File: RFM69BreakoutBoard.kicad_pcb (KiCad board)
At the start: 2 copper layers, 25.7 x 25.4 mm, 16 parts, among them P1 CONN_7, U1 MCP1703, U2 74LVC2, U3 74AHC1G, U4 RFM69HW

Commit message: clean up
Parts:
- removed D2, D3: LED-GREEN, LED-0805
- removed R3, R4: 0, SM0805
- removed R5: 270, SM0805
- removed U4: RFM69HW, RFM69HW
- added C4: 10u, 10uCap, F.Cu at (107.4, 150.2)
- added C5: .1u, SM0805, F.Cu at (99.6, 149.1)
- added P11: ANA hole, PINTST, F.Cu at (106.7, 143.0)
- added W1: TEST, SMTST, F.Cu at (82.9, 158.9)
- added W2: TEST, SMTST, F.Cu at (102.7, 158.8)
- added W3: TEST, SMTST, F.Cu at (98.0, 158.9)
- added W4: TEST, SMTST, F.Cu at (107.3, 158.9)
- added W5: TEST, SMTST, F.Cu at (93.1, 158.9)
- added W6: TEST, SMTST, F.Cu at (88.0, 158.9)
- added W7: TEST, SMTST, F.Cu at (90.2, 141.1)
- added W8: TEST, SMTST, F.Cu at (94.6, 141.0)
- added W9: TEST, SMTST, F.Cu at (99.4, 141.0)
- C1, C3, U1: moved to F.Cu
- C2: footprint SM0805 -> 10uCap; moved to F.Cu
- D1: value LED-GREEN -> LED
- P1: value CONN_7 -> BB Holes
- R1: value 270 -> 10K; moved to F.Cu
- R2: value 270 -> 470; moved to F.Cu
- U2: value 74LVC2 -> 74LVC245; moved to F.Cu
- U3: value 74AHC1G -> RFM69HW; footprint SOT353 -> RFM69HW
- moved R1 19.2 mm to (89.5, 155.4), turned to 90 degrees
- moved U3 14.7 mm to (94.7, 147.3), turned to 0 degrees
- moved R2 11.2 mm to (99.3, 143.9), turned to 0 degrees
- moved C2 9.88 mm to (82.8, 150.0)
- moved C3 9.44 mm to (95.5, 151.6)
- moved D1 9.25 mm to (99.1, 146.1)
- moved U1 9.02 mm to (93.1, 152.1), turned to 180 degrees
- moved U2 8.81 mm to (92.8, 146.6), turned to 0 degrees
- moved C1 6.59 mm to (95.5, 153.8)
- moved P1 0.28 mm to (95.8, 162.8)
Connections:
- D1 pad 1: /MISO -> N-0000010
- D1 pad 2: /LED -> N-0000011
- P1 pad 1: /5V -> +5V
- P1 pad 3: /CLK -> /CLK_5V
- P1 pad 5: /MOSI -> /MOSI_5V
- P1 pad 6: /CS -> /CS_5V
- R1 pad 1: /LED -> /CS_5V
- R1 pad 2: GND -> +5V
- R2 pad 1: /LED -> N-0000011
- R2 pad 2: GND -> /CS_3V3
- U2 pad 1: (no net) -> +3.3V
- U2 pad 15: (no net) -> N-0000010
- U2 pad 16: /CS -> /CS_3V3
- U2 pad 17: /MOSI -> /MOSI_3V3
- U2 pad 18: /CLK -> /CLK_3V3
- U2 pad 2: /CLK -> N-000004
- U2 pad 3: /MOSI -> N-000007
- U2 pad 4: /CS -> N-000008
- U2 pad 5: (no net) -> N-000004
- U2 pad 6: (no net) -> GND
- U2 pad 7: (no net) -> GND
- U2 pad 8: (no net) -> GND
- U2 pad 9: (no net) -> GND
- U3 pad 1: /CS -> (no net)
- U3 pad 2: /MISO -> N-000001
- U3 pad 3: GND -> (no net)
- U3 pad 4: /MISO -> (no net)
- U3 pad 5: +3.3V -> (no net)
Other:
- board size 25.7 x 25.4 mm -> 30 x 25.9 mm

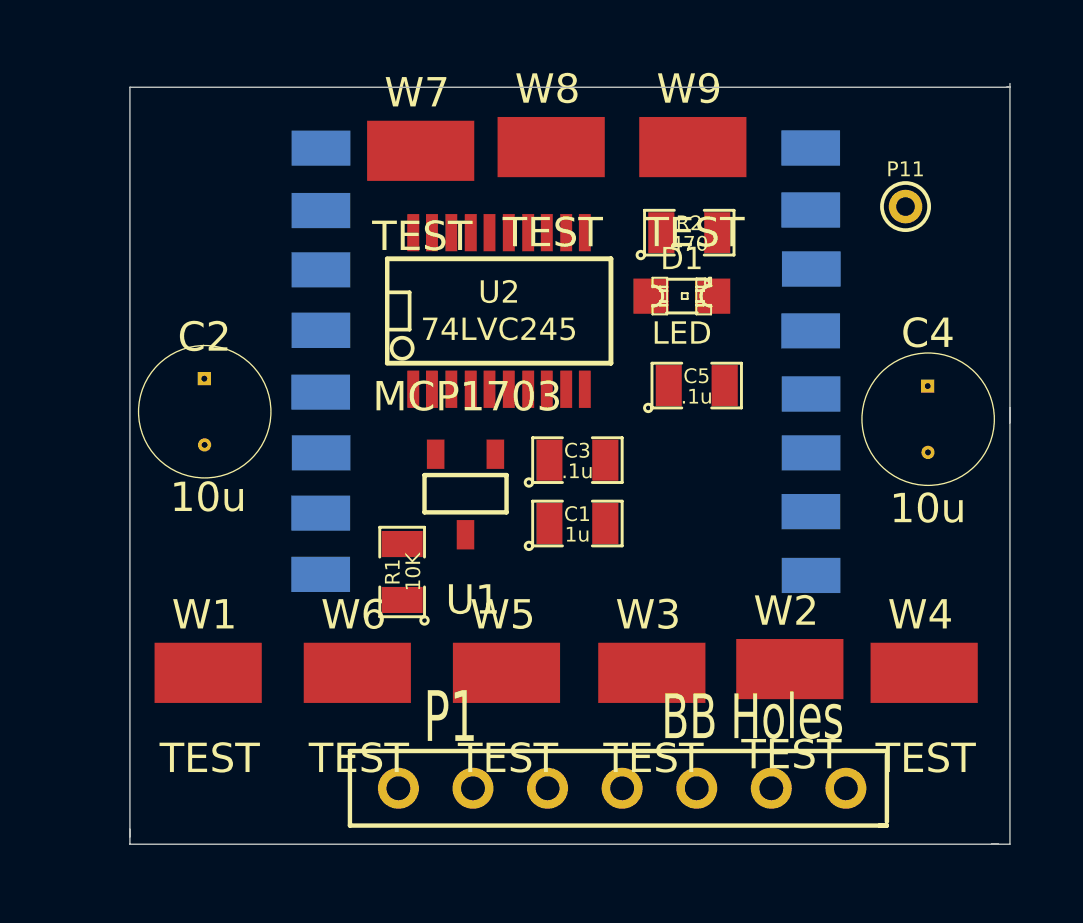
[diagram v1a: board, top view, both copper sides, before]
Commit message: started work on pcb layout
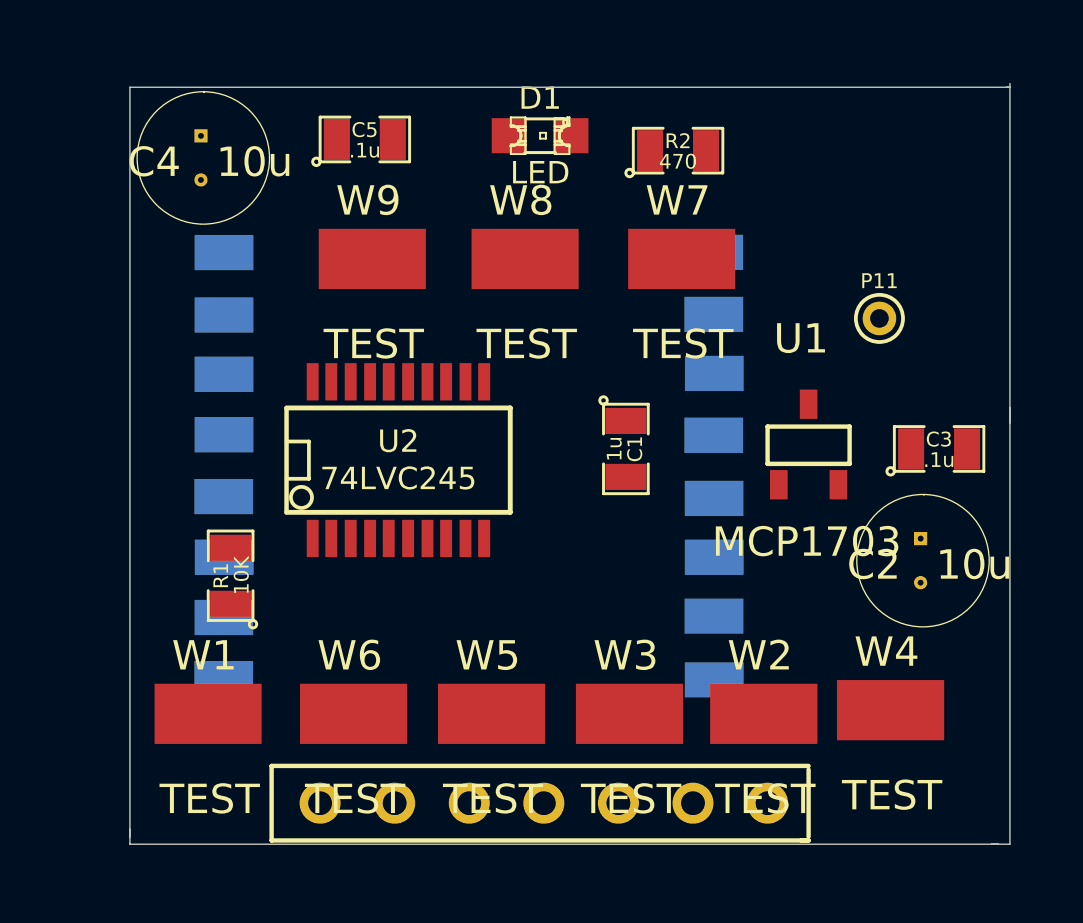
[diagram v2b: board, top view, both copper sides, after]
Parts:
- removed P1: BB Holes, 7_PINS
- added ?: , 7_PINS, F.Cu at (93.1, 163.3)
- moved C4 26.2 mm to (82.7, 141.6)
- moved C2 25.0 mm to (107.2, 155.3)
- moved C5 14.1 mm to (88.3, 140.7)
- moved C3 12.3 mm to (107.8, 151.3)
- moved W9 11.6 mm to (88.5, 144.8)
- moved W7 9.62 mm to (99.1, 144.8)
- moved U1 8.90 mm to (102.0, 151.8), turned to 0 degrees
- moved D1 7.29 mm to (94.2, 140.6)
- moved U2 6.13 mm to (89.4, 151.6)
- moved R1 5.84 mm to (83.7, 155.6)
- moved U3 4.85 mm to (91.4, 150.9)
- moved P11 3.91 mm to (105.8, 146.8)
- moved W8 3.91 mm to (93.7, 144.8)
- moved C1 3.03 mm to (97.2, 151.3), turned to 270 degrees
- moved R2 2.82 mm to (98.9, 141.1)
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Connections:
- net N-0000032 renamed /ANA
- D1 pad 1: N-0000010 -> /CLK_3V3
- D1 pad 2: N-0000011 -> /CLK_3V3
- R2 pad 1: N-0000011 -> /CLK_3V3
- U2 pad 15: N-0000010 -> /CLK_3V3
- U2 pad 2: N-000004 -> /CLK_5V
- U2 pad 3: N-000007 -> /MOSI_5V
- U2 pad 4: N-000008 -> /CS_5V
- U2 pad 5: N-000004 -> /CLK_5V
- U3 pad 11: N-000003 -> GND
- U3 pad 12: /CS_3V3 -> /CLK_3V3
- U3 pad 13: N-000006 -> /MISO
- U3 pad 14: N-000005 -> /MOSI_3V3
- U3 pad 15: N-000002 -> /CS_3V3
- U3 pad 2: N-000001 -> /INT
- U3 pad 9: N-000003 -> GND

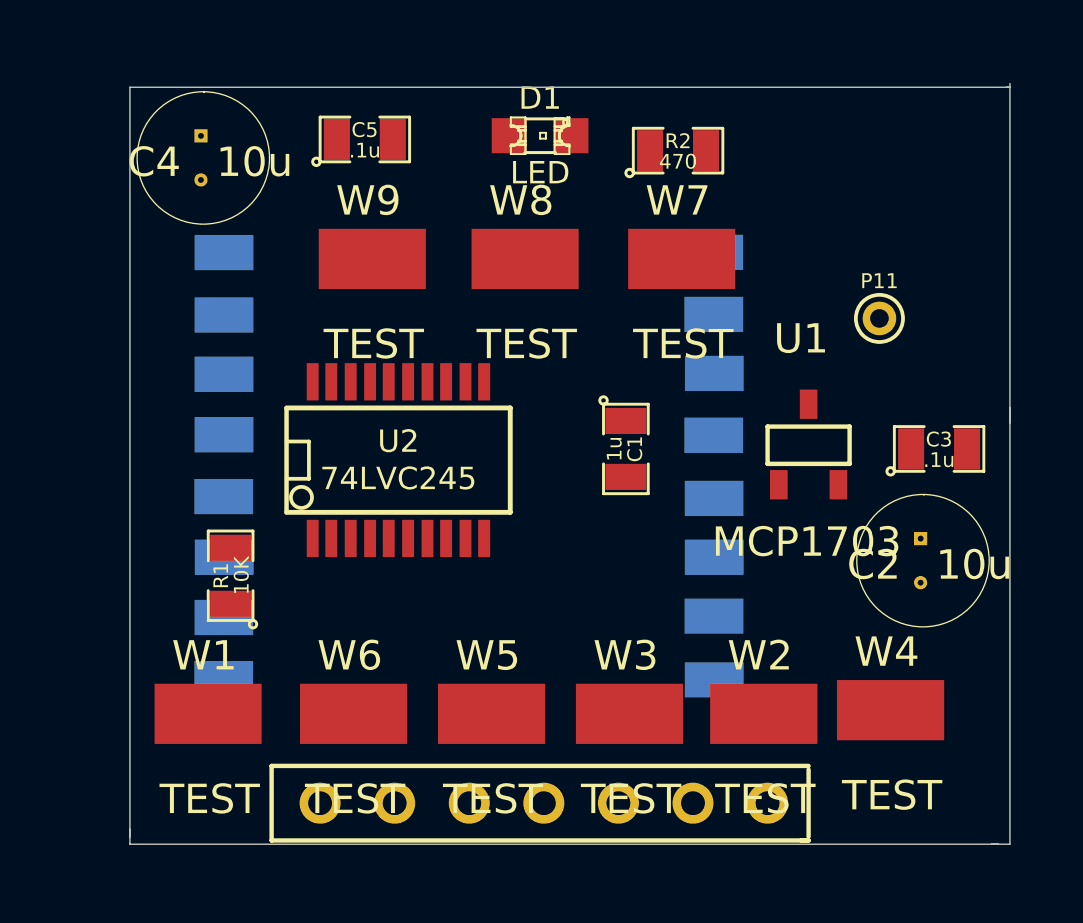
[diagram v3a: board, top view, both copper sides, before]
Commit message: update to chip layout (PCBnew)
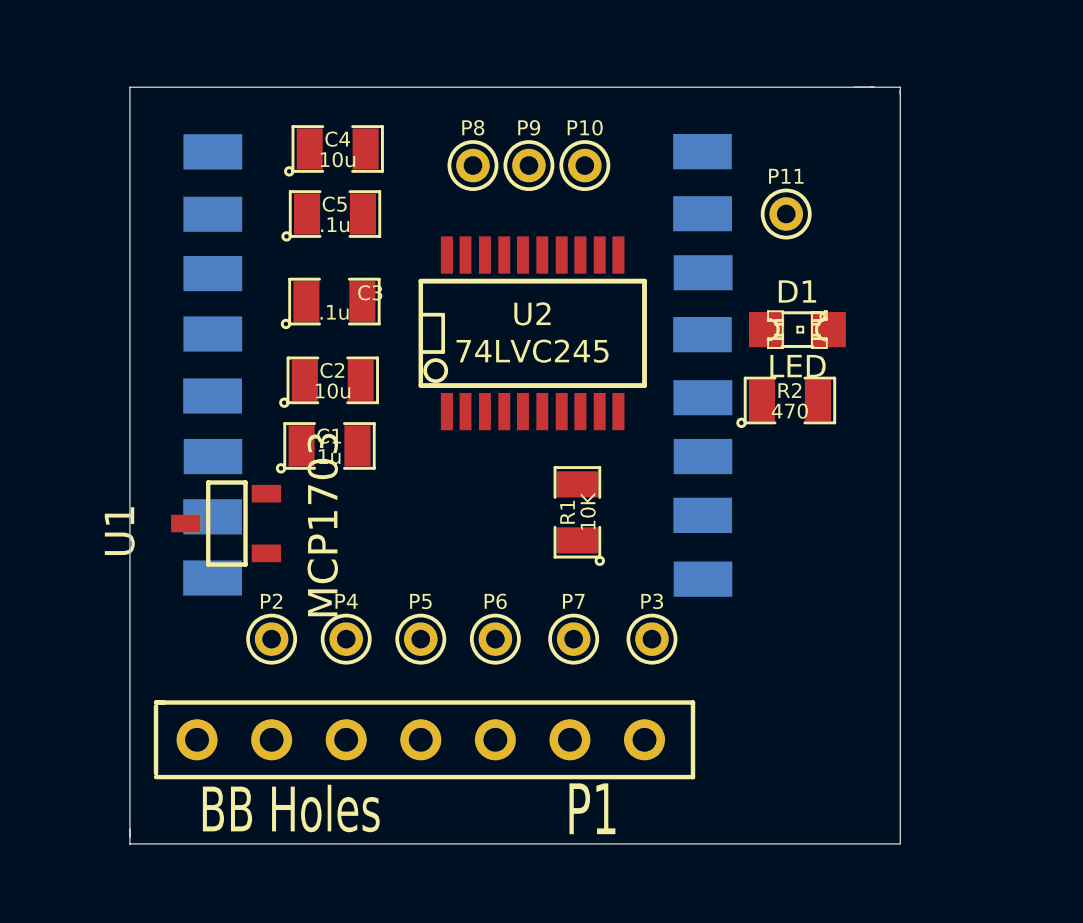
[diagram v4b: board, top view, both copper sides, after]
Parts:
- removed ?: , 7_PINS
- removed W1, W2, W3, W4, W5, W6, W7, W8, W9: TEST, SMTST
- added P1: BB Holes, 7_PINS, F.Cu at (91.4, 161.2)
- added P10: TST, PINTST, F.Cu at (95.8, 141.6)
- added P2: TST, PINTST, F.Cu at (85.1, 157.7)
- added P3: TST, PINTST, F.Cu at (98.0, 157.7)
- added P4: TST, PINTST, F.Cu at (87.6, 157.7)
- added P5: TST, PINTST, F.Cu at (90.2, 157.7)
- added P6: TST, PINTST, F.Cu at (92.7, 157.7)
- added P7: TST, PINTST, F.Cu at (95.4, 157.7)
- added P8: TST, PINTST, F.Cu at (91.9, 141.6)
- added P9: TST, PINTST, F.Cu at (93.9, 141.6)
- C2, C4: footprint 10uCap -> SM0805
- moved C3 21.2 mm to (87.2, 146.2)
- moved C2 21.0 mm to (87.2, 148.9)
- moved U1 18.1 mm to (84.2, 155.2), turned to 90 degrees
- moved R1 12.0 mm to (95.5, 153.4)
- moved D1 11.0 mm to (103.0, 147.2)
- moved C1 10.1 mm to (87.1, 151.2), turned to 0 degrees
- moved R2 9.32 mm to (102.7, 149.6)
- moved U2 6.29 mm to (94.0, 147.3)
- moved P11 4.77 mm to (102.6, 143.3)
- moved C4 4.70 mm to (87.3, 141.0)
- moved U3 3.45 mm to (91.1, 147.4)
- moved C5 2.74 mm to (87.2, 143.3)
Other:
- board size 30 x 25.9 mm -> 26.2 x 25.8 mm

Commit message: removed 74LVC245 level shifter.  Replaced with 74HCT125
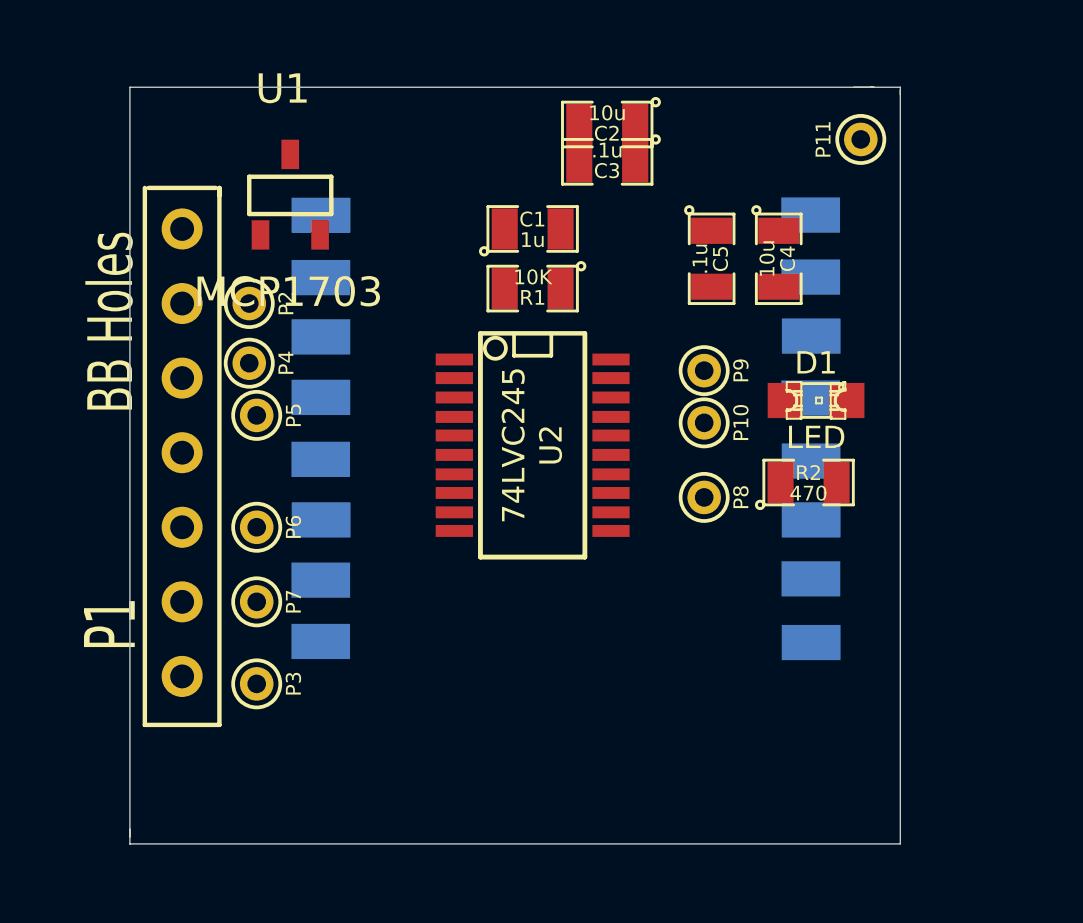
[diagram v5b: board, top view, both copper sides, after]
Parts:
- moved C4 15.5 mm to (102.4, 144.8), turned to 270 degrees
- moved P8 13.8 mm to (99.8, 152.9), turned to 270 degrees
- moved P3 13.5 mm to (84.6, 159.3), turned to 270 degrees
- moved C5 12.9 mm to (100.1, 144.8), turned to 270 degrees
- moved C2 12.8 mm to (96.5, 140.2), turned to 180 degrees
- moved P1 12.7 mm to (82.0, 152.7), turned to 90 degrees
- moved U1 11.9 mm to (84.3, 143.3), turned to 0 degrees
- moved P2 11.5 mm to (84.3, 146.3), turned to 270 degrees
- moved P7 10.9 mm to (84.6, 156.5), turned to 270 degrees
- moved C3 10.4 mm to (96.5, 141.5), turned to 180 degrees
- moved C1 10.1 mm to (94.0, 143.8)
- moved P4 9.96 mm to (84.3, 148.3), turned to 270 degrees
- moved P10 9.66 mm to (99.8, 150.4), turned to 270 degrees
- moved P5 9.45 mm to (84.6, 150.1), turned to 270 degrees
- moved P9 9.19 mm to (99.8, 148.6), turned to 270 degrees
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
